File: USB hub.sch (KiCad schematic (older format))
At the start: 48 parts, among them IC1 24SN, IC2 FE1.1S, J2 USB_C2-LAYER, J3 USB_A_SMT_FEMALE, J4 USB_A_SMT_FEMALE, J5 USB_A_SMT_FEMALE, X1 12MHz

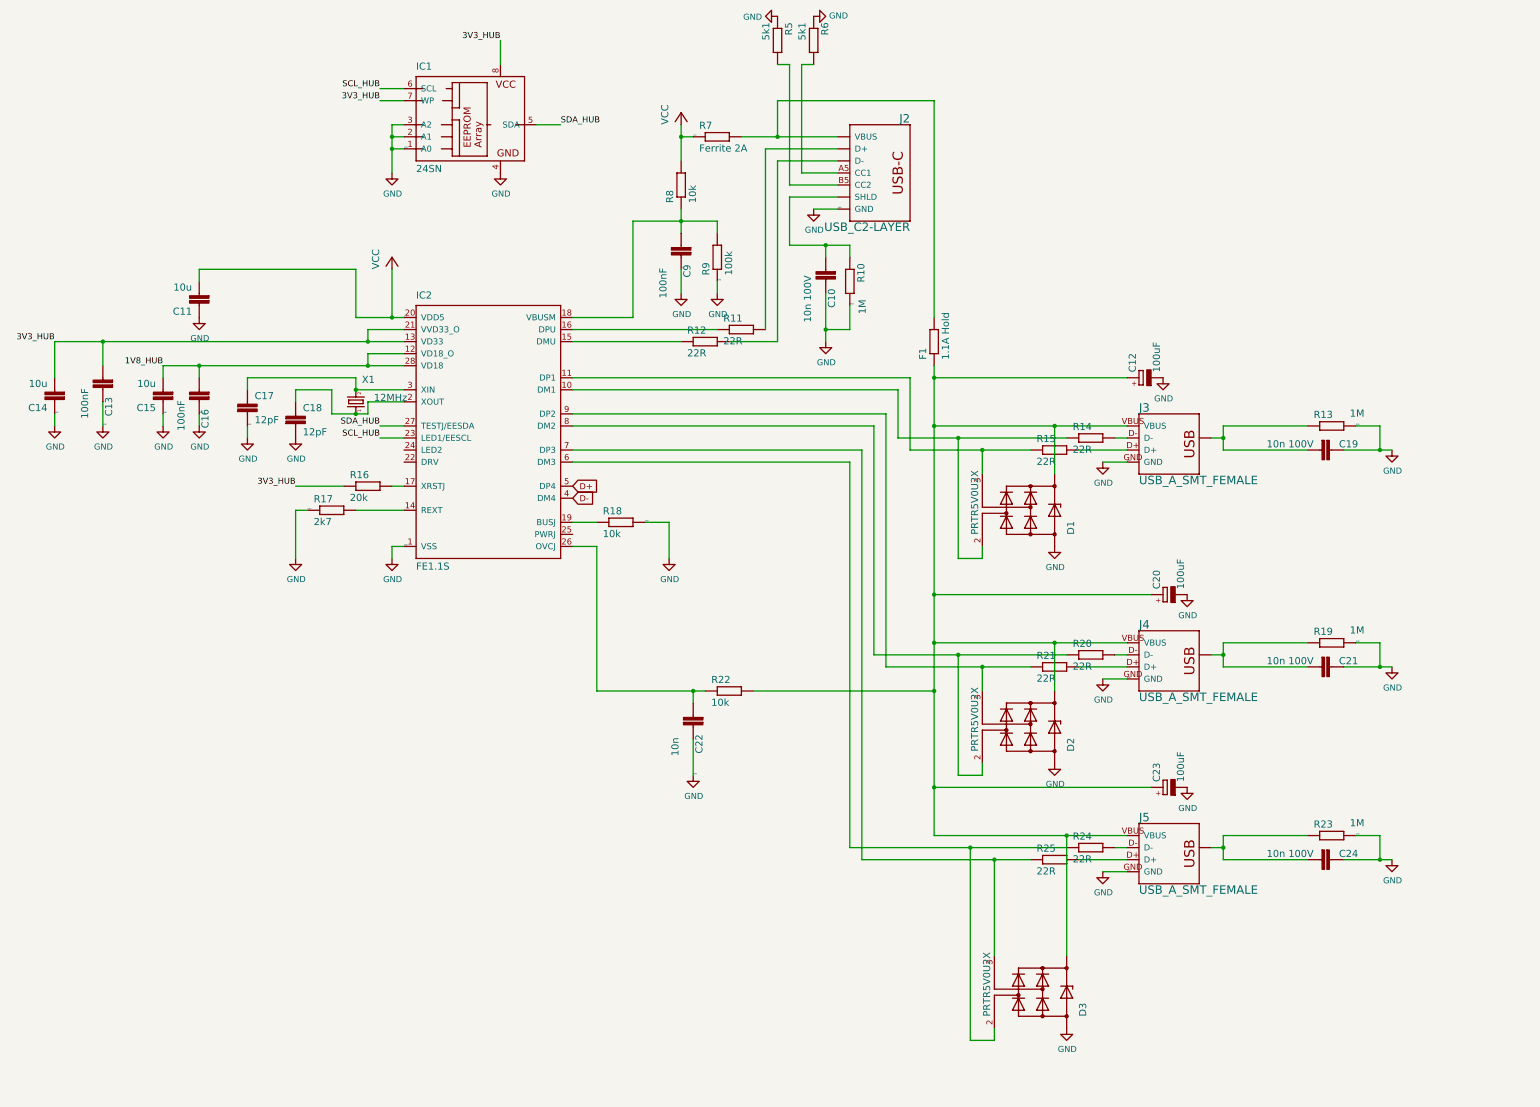
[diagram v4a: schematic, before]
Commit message: add daughter board
Updated schematic and pcb to remove onboard usb c nd replace with connector to use unified C board
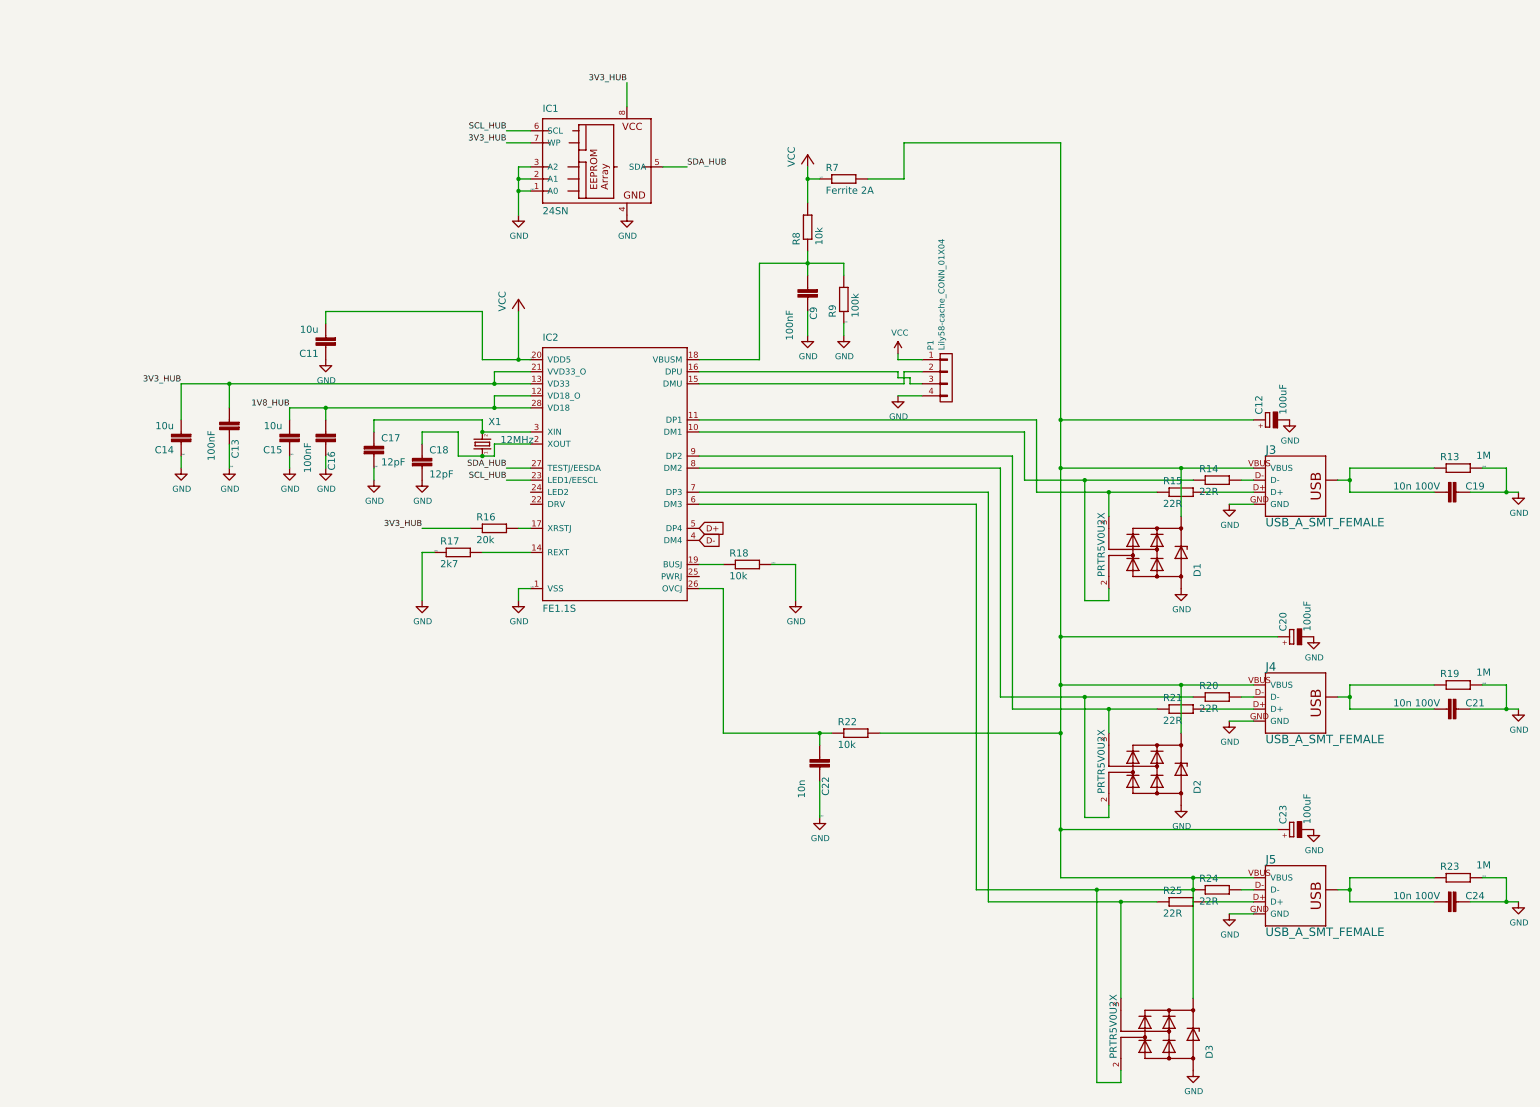
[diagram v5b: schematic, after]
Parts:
- removed C10: 10n 100V, Capacitor_SMD:C_0805_2012Metric, symbol hub_keyboard-eagle-import:C-EUC0603
- removed F1: 1.1A Hold, Fuse:Fuse_1206_3216Metric, symbol hub_keyboard-eagle-import:R-EU_R1210
- removed J2: USB_C2-LAYER, hub_keyboard:USB-C-16P, symbol hub_keyboard-eagle-import:USB_C2-LAYER
- removed R10: 1M, 1_Keyboard Footprints:R_0603, symbol hub_keyboard-eagle-import:R-EU_R0603
- removed R11, R12: 22R, 1_Keyboard Footprints:R_0603, symbol hub_keyboard-eagle-import:R-EU_R0603
- removed R5, R6: 5k1, 1_Keyboard Footprints:R_0603, symbol hub_keyboard-eagle-import:R-EU_R0603
- added P1: Lily58-cache_CONN_01X04, 1_Keyboard Footprints:JST-SR-4, symbol Lily58-cache:Lily58-cache_CONN_01X04
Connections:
- net GND: now also P1.4 (P4)
- net VCC: now also P1.1 (P1)
- net at C12.+, C20.+, C23.+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: now also D3.2 (IO1), IC2.6 (DM3), R24.1, R7.2
- net at IC2.15 (DMU): now also P1.2 (P2)
- net at IC2.16 (DPU): now also P1.3 (P3)
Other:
- moved on the sheet: C11, C12, C13, C14, C15, C16, C17, C18, C19, C20, C21, C22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
